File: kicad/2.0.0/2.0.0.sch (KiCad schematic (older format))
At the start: 39 parts

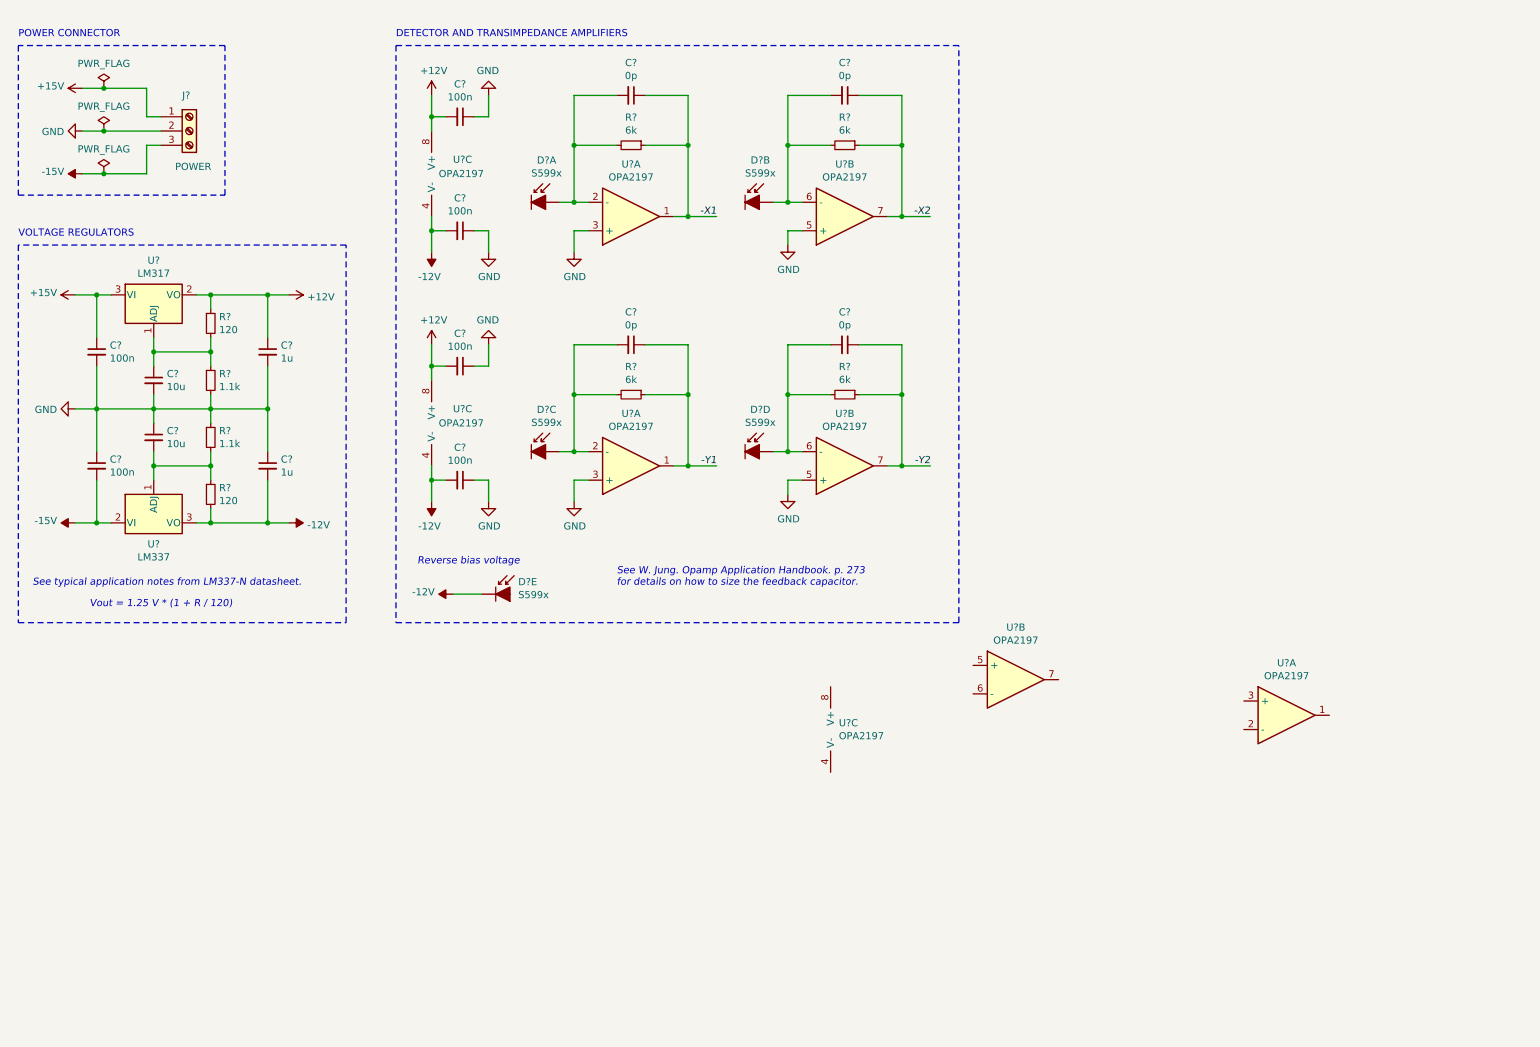
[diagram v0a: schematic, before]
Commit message: completed schematic of revision 2.0.0
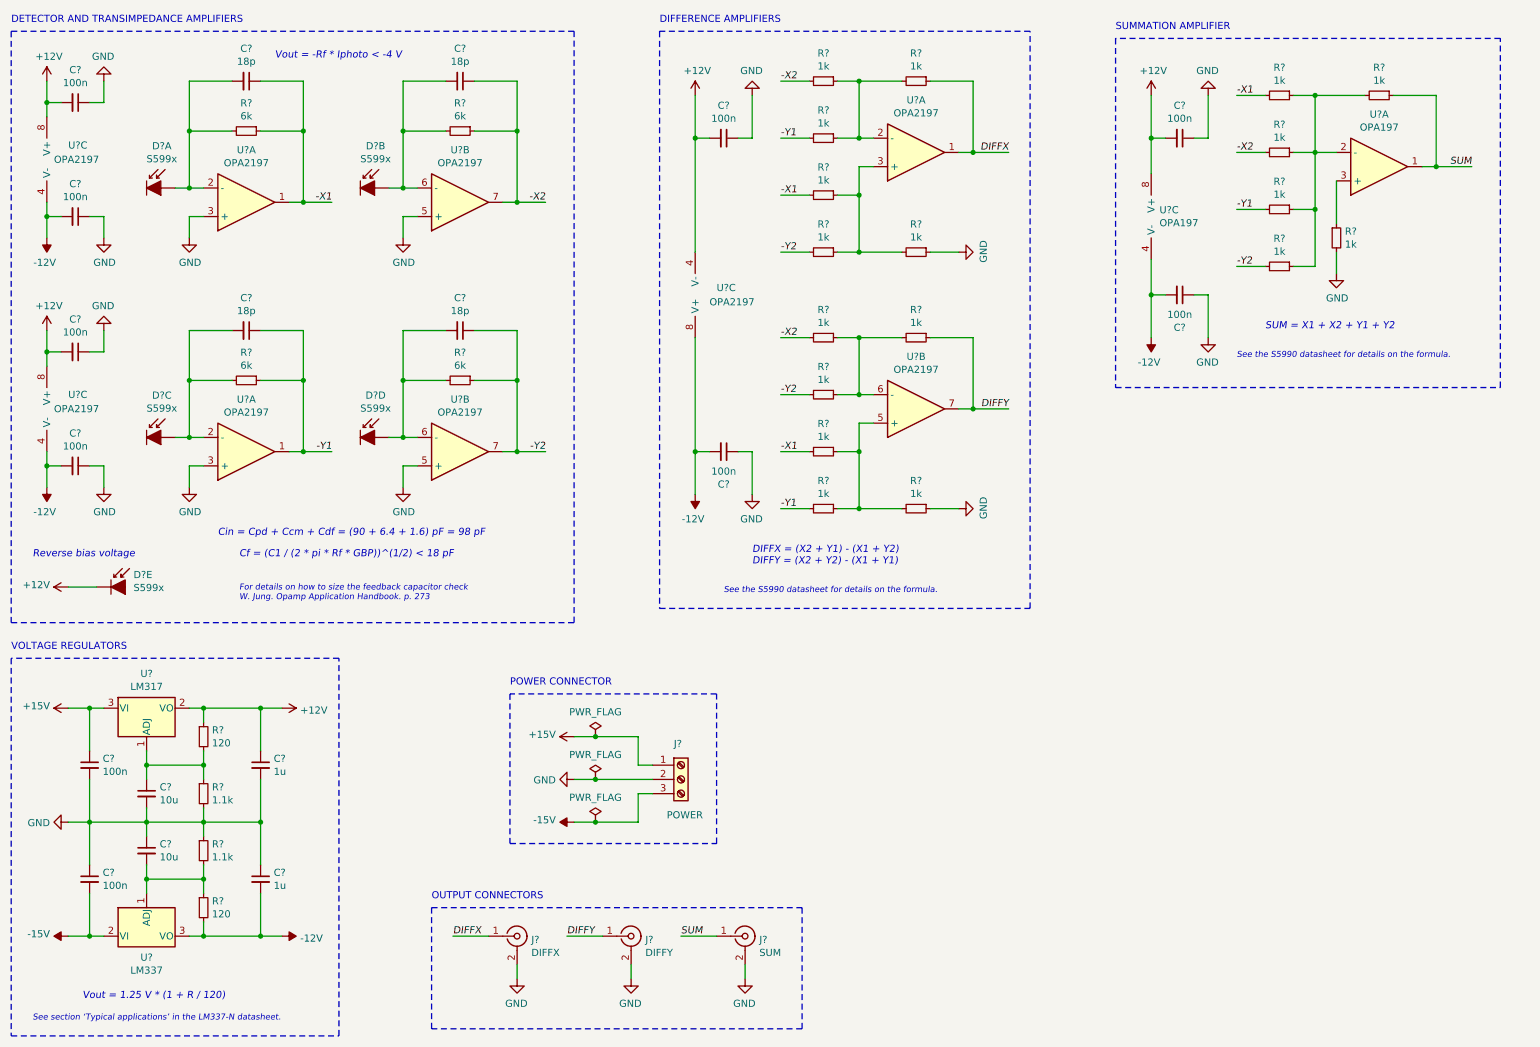
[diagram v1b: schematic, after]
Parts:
- added C? (x4): 100n, symbol Device:C_Small
- added J?: DIFFX, symbol Connector:Conn_Coaxial
- added J?: DIFFY, symbol Connector:Conn_Coaxial
- added J?: SUM, symbol Connector:Conn_Coaxial
- added R? (x18): 1k, symbol Device:R_Small
- added U? (x2): OPA197, symbol Device:Opamp_Dual_Generic
- C? (x4): value 0p -> 18p
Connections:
- net +12V: now also D?.8 (K), U?.4 (V-), C?.2, C?.2, U?.8 (V+)
- net -12V: now also U?.8 (V+), C?.2, C?.2, U?.4 (V-); no longer D?.8 (K)
- net -X1: now also R?.2, R?.2, R?.2
- net -X2: now also R?.2, R?.2, R?.2
- net -Y1: now also R?.2, R?.2, R?.2
- net -Y2: now also R?.2, R?.2, R?.2
- net GND: now also C?.1, C?.1, C?.1, C?.1, J?.2 (Ext), J?.2 (Ext), J?.2 (Ext), R?.1, R?.1, R?.2
- net DIFFX: now reaches U?.1
- net DIFFX: now also J?.1 (In), R?.1
- net at U?.2 (-): now also R?.1, R?.1, R?.2
- net at U?.3 (+): now also R?.1, R?.1, R?.2
- net at U?.5 (+): now also R?.1, R?.1, R?.2
- net at U?.6 (-): now also R?.1, R?.1, R?.2
- net DIFFY: now reaches U?.7
- net DIFFY: now also J?.1 (In), R?.1
- new net: R?.1, R?.1, R?.1, R?.1, R?.2, U?.2 (-)
- new net: R?.1, U?.3 (+)
- new net SUM: J?.1 (In), R?.1, U?.1
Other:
- note added: "Cf = (C1 / (2 * pi * Rf * GBP))^(1/2) < 18 pF"
- note added: "Cin = Cpd + Ccm + Cdf = (90 + 6.4 + 1.6) pF = 98 pF"
- note added: "DIFFERENCE AMPLIFIERS"
- note added: "DIFFX = (X2 + Y1) - (X1 + Y2)\nDIFFY = (X2 + Y2) - (X1 + Y1)"
- note added: "For details on how to size the feedback capacitor check\nW. Jung. Opamp Application Handbook. p. 273"
- note added: "OUTPUT CONNECTORS"
- note added: "SUM = X1 + X2 + Y1 + Y2"
- note added: "SUMMATION AMPLIFIER"
- note added: "See section ‘Typical applications’ in the LM337-N datasheet."
- note added: "See the S5990 datasheet for details on the formula."
- note added: "Vout = -Rf * Iphoto < -4 V"
- note removed: "See W. Jung. Opamp Application Handbook. p. 273\nfor details on how to size the feedback capacitor."
- note removed: "See typical application notes from LM337-N datasheet."
- moved on the sheet: C?, D?A, D?B, D?C, D?D, D?E, J?, R?, U?, U?A, U?B, U?C
